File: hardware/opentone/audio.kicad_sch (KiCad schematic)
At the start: 29 parts

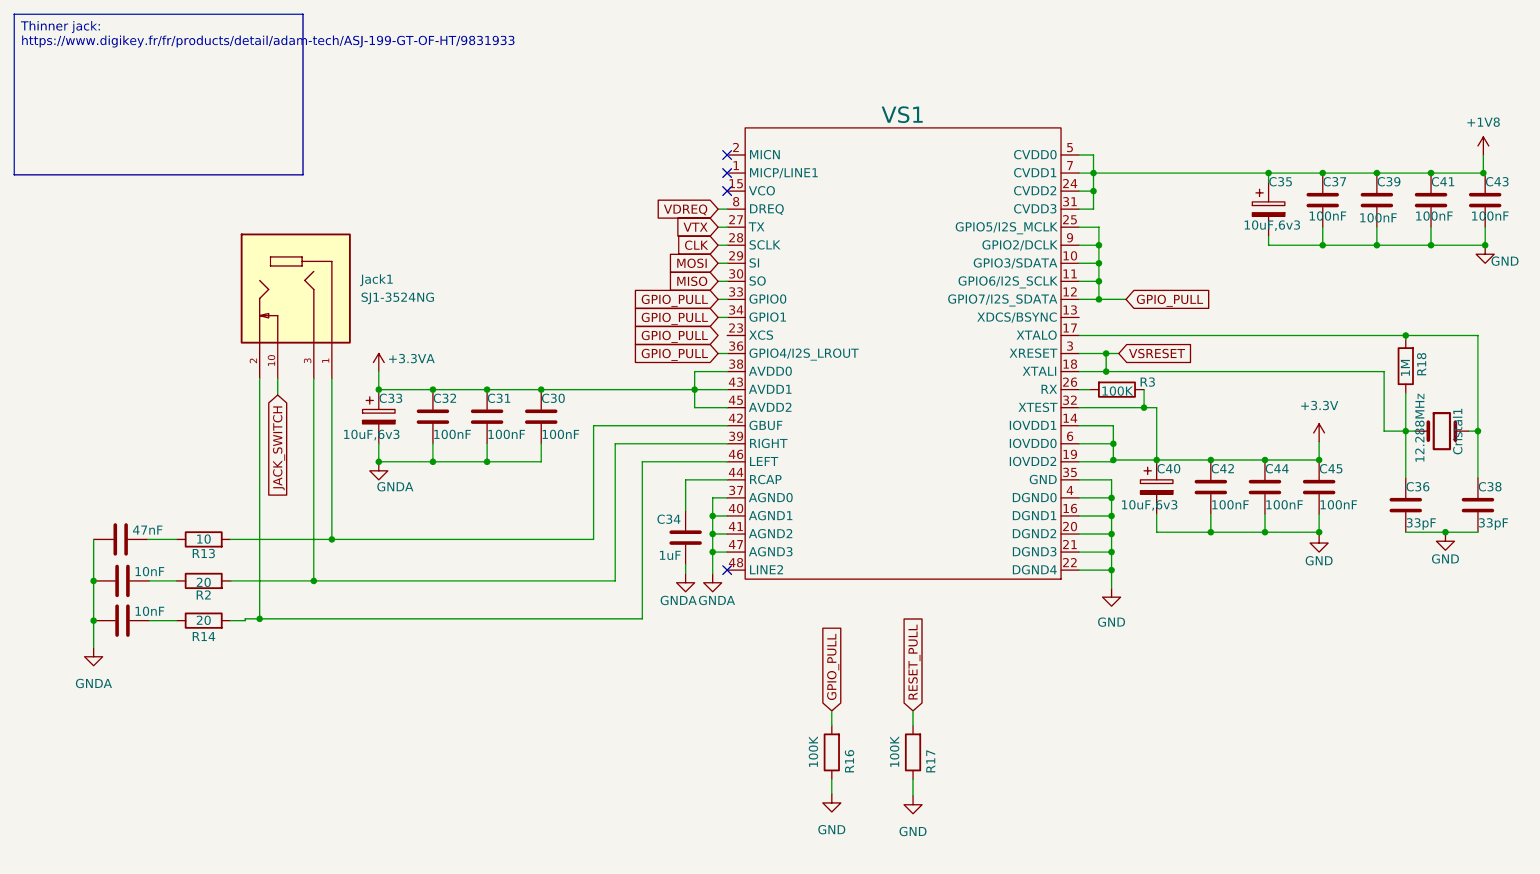
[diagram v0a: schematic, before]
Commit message: devboard audio and bluetooth schema
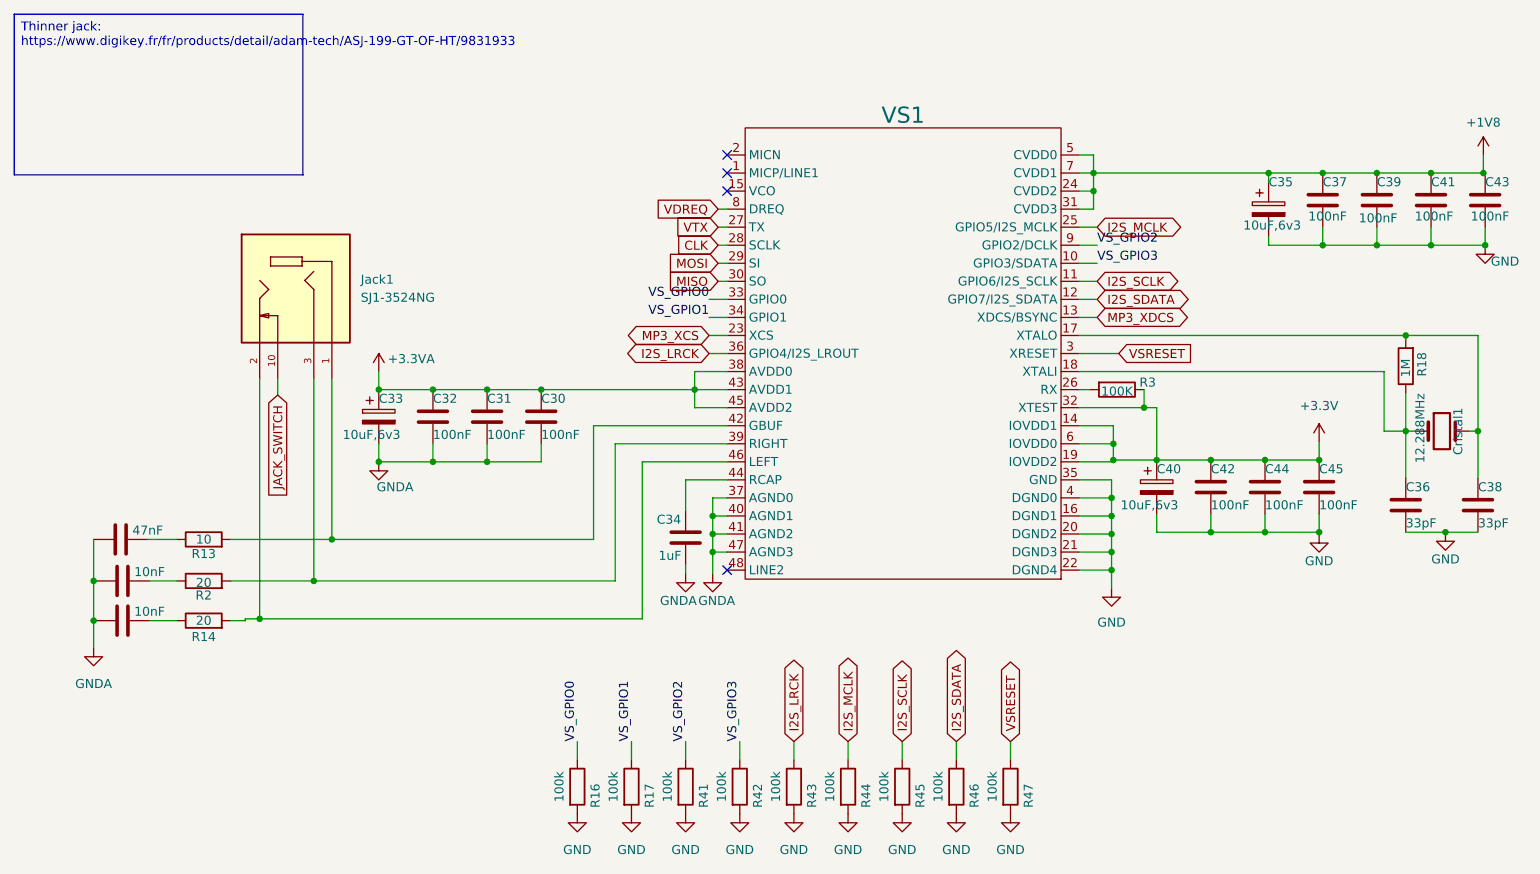
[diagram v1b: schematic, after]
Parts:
- added R41, R42, R43, R44, R45, R46, R47: 100k, symbol Device:R
- R16, R17: value 100K -> 100k
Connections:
- net RESET_PULL is gone; now on net GND: R17.2
- net GND: now also R16.2, R41.2, R42.2, R43.2, R44.2, R45.2, R46.2, R47.2; no longer R16.1, R17.1
- net VSRESET: now also R47.1; no longer C36.1, Cristal1.1, R18.1, VS1.18 (XTALI)
- net MP3_XDCS: now reaches VS1.13 (XDCS/BSYNC)
- net MP3_XCS: now reaches VS1.23 (XCS)
- removed net GPIO_PULL: R16.2, VS1.10 (GPIO3/SDATA), VS1.11 (GPIO6/I2S_SCLK), VS1.12 (GPIO7/I2S_SDATA), VS1.25 (GPIO5/I2S_MCLK), VS1.33 (GPIO0), VS1.34 (GPIO1), VS1.36 (GPIO4/I2S_LROUT), VS1.9 (GPIO2/DCLK)
- new net: C36.1, Cristal1.1, R18.1, VS1.18 (XTALI)
- new net I2S_LRCK: R43.1, VS1.36 (GPIO4/I2S_LROUT)
- new net I2S_MCLK: R44.1, VS1.25 (GPIO5/I2S_MCLK)
- new net I2S_SCLK: R45.1, VS1.11 (GPIO6/I2S_SCLK)
- new net I2S_SDATA: R46.1, VS1.12 (GPIO7/I2S_SDATA)
- new net VS_GPIO0: R16.1, VS1.33 (GPIO0)
- new net VS_GPIO1: R17.1, VS1.34 (GPIO1)
- new net VS_GPIO2: R41.1, VS1.9 (GPIO2/DCLK)
- new net VS_GPIO3: R42.1, VS1.10 (GPIO3/SDATA)

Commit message: wiring main MCU
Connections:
- net CLK renamed SPI2_SCK
- net JACK_SWITCH renamed HP1_DET
- net MISO renamed SPI2_MISO
- net MOSI renamed SPI2_MOSI
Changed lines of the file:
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@@
 		)
 	)
-	(global_label "CLK"
+	(global_label "SPI2_SCK"
 		(shape input)
 		(at 134.112 63.5 180)
@@
 		)
 	)
-	(global_label "MOSI"
+	(global_label "SPI2_MOSI"
 		(shape input)
 		(at 134.112 66.04 180)
@@
 		)
 	)
-	(global_label "JACK_SWITCH"
+	(global_label "HP1_DET"
 		(shape input)
 		(at 72.136 84.582 270)
@@
 		)
 	)
-	(global_label "MISO"
+	(global_label "SPI2_MISO"
 		(shape input)
 		(at 134.112 68.58 180)

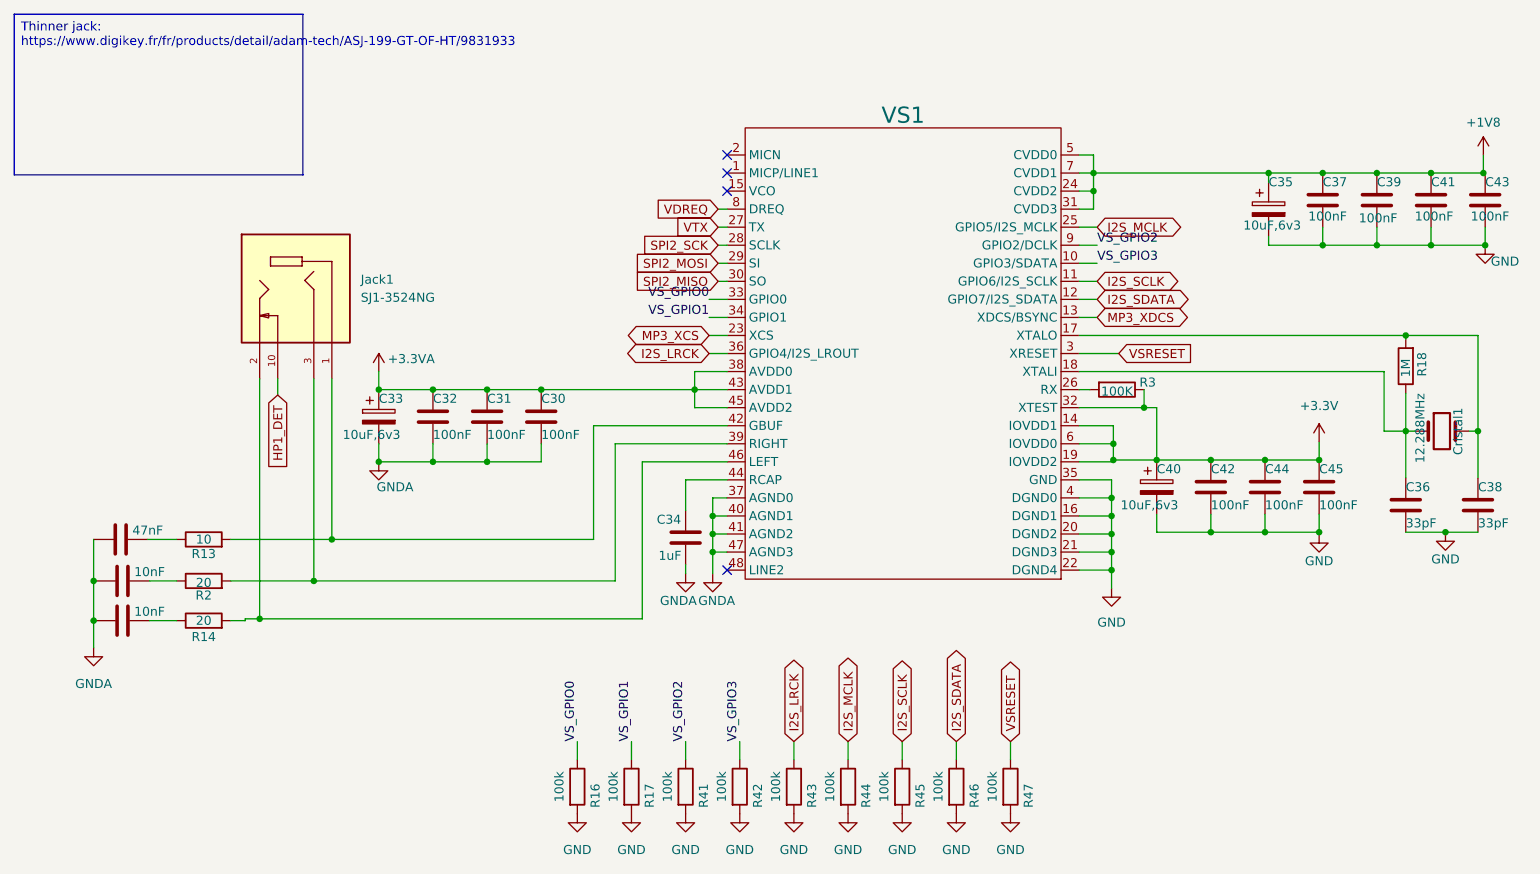
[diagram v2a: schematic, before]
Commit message: added sd card, haptic, updated old parts and set a datasheet and MPN to all parts
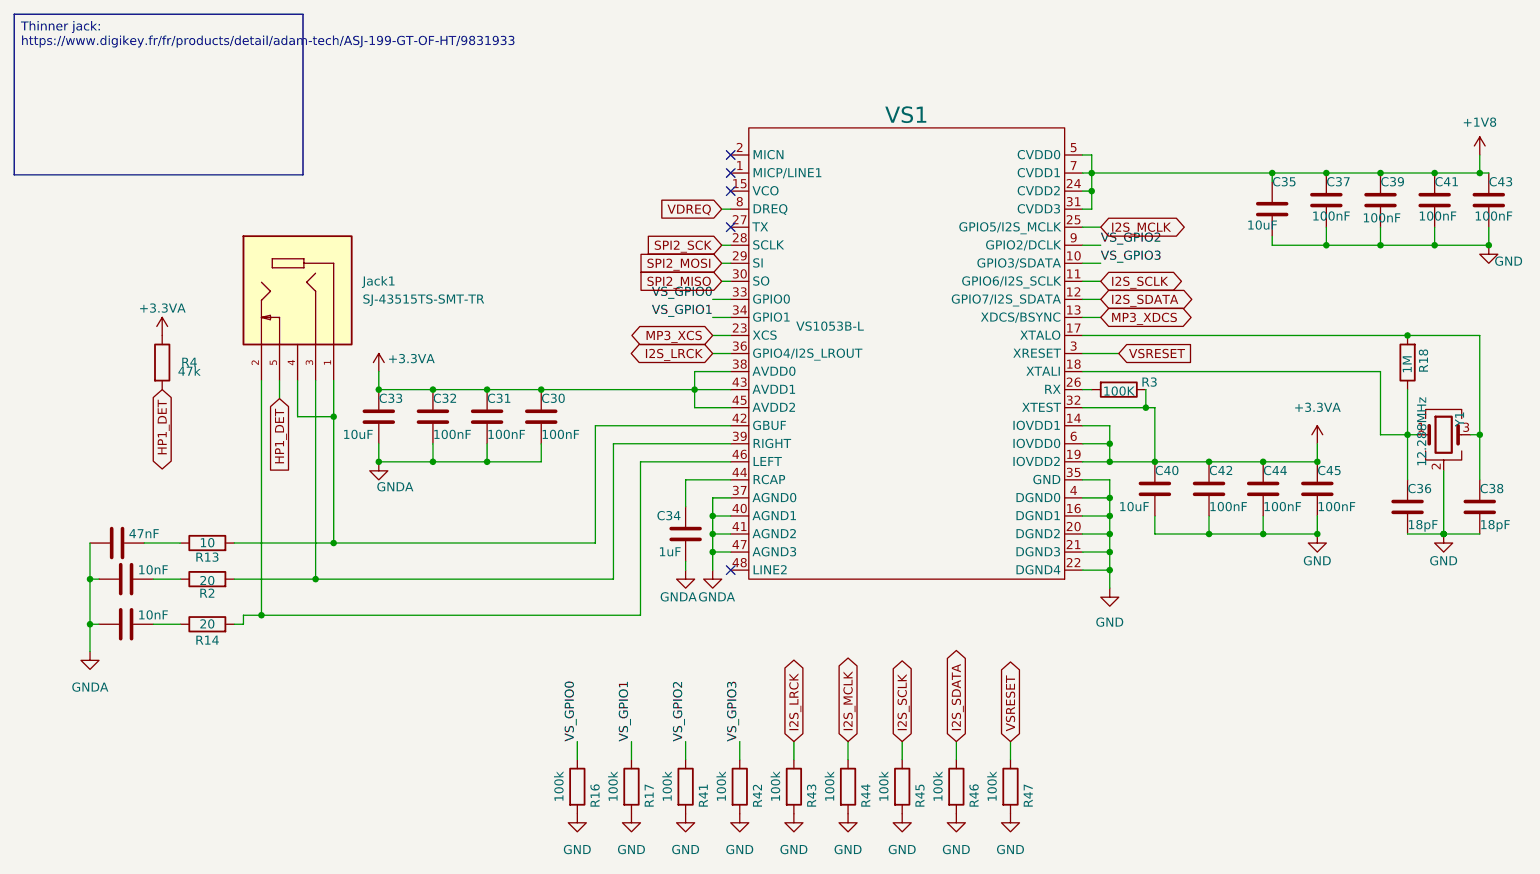
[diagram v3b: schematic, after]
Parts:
- added R4: 47k, Resistor_SMD:R_0603_1608Metric, symbol Device:R
- C29, C3: footprint (none) -> Capacitor_SMD:C_0603_1608Metric; LCSC (none) -> C85973; Manufacturer (none) -> Murata; Part number (none) -> GRM1885C1H103JA01D
- C30, C31, C32, C37, C39, C41, C42, C43, C44, C45: footprint (none) -> Capacitor_SMD:C_0603_1608Metric; LCSC (none) -> C14663; Manufacturer (none) -> YAGEO; Part number (none) -> CC0603KRX7R9BB104
- C33, C35, C40: value 10uF,6v3 -> 10uF; footprint (none) -> Capacitor_SMD:C_0603_1608Metric; symbol Device:C_Polarized -> Device:C; LCSC (none) -> C19702; Manufacturer (none) -> Samsung Electro-Mechanics; Part number (none) -> CL10A106KP8NNNC
- C34: footprint (none) -> Capacitor_SMD:C_0603_1608Metric; LCSC (none) -> C15849; Manufacturer (none) -> Samsung Electro-Mechanics; Part number (none) -> CL10A105KB8NNNC
- C36, C38: value 33pF -> 18pF; footprint (none) -> Capacitor_SMD:C_0603_1608Metric; LCSC (none) -> C1647; Manufacturer (none) -> Samsung Electro-Mechanics; Part number (none) -> CL10C180JB8NNNC
- C9: footprint (none) -> Capacitor_SMD:C_1206_3216Metric; LCSC (none) -> C21812; Manufacturer (none) -> Murata; Part number (none) -> GRM31M5C1H473JA01L
- Jack1: value SJ1-3524NG -> SJ-43515TS-SMT-TR; footprint opentone:CUI_SJ1-3524NG -> opentone:CUI_SJ-43515TS-SMT-TR; symbol opentone:SJ1-3524NG -> opentone:SJ-43515TS-SMT-TR; LCSC (none) -> C5353507; Part number SJ1-3524NG -> SJ-43515TS-SMT-TR
- R13: footprint (none) -> Resistor_SMD:R_0603_1608Metric; LCSC (none) -> C22859; Manufacturer (none) -> UNI-ROYAL; Part number (none) -> 0603WAF100JT5E
- R14, R2: footprint (none) -> Resistor_SMD:R_0603_1608Metric; LCSC (none) -> C22950; Manufacturer (none) -> UNI-ROYAL; Part number (none) -> 0603WAF200JT5E
- R16, R17, R3, R41, R42, R43, R44, R45, R46, R47: footprint (none) -> Resistor_SMD:R_0603_1608Metric; LCSC (none) -> C25803; Manufacturer (none) -> UNI-ROYAL; Part number (none) -> 0603WAF1003T5E
- R18: footprint (none) -> Resistor_SMD:R_0603_1608Metric; LCSC (none) -> C22935; Manufacturer (none) -> UNI-ROYAL; Part number (none) -> 0603WAF1004T5E
- VS1: value ~ -> VS1053B-L; footprint (none) -> Package_QFP:LQFP-48_7x7mm_P0.5mm; LCSC (none) -> C9922; Manufacturer (none) -> VLSI Solution; Part number (none) -> VS1053B-L
- Y1: renamed from Cristal1; footprint (none) -> Crystal:Crystal_SMD_3225-4Pin_3.2x2.5mm; symbol Device:Crystal -> Device:Crystal_GND24; LCSC (none) -> C362472; Manufacturer (none) -> Yajingxin; Part number (none) -> TXM12.288M0004322FBCDO00T
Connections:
- net +3.3V is gone; now on net +3.3VA: C40.1, C42.1, C44.1, C45.1, R3.1, VS1.14 (IOVDD1), VS1.19 (IOVDD2), VS1.32 (XTEST), VS1.6 (IOVDD0)
- net +3.3VA: now also R4.1
- net GND: now also Y1.2 (G), Y1.4 (G)
- net HP1_DET: now also Jack1.5, R4.2; no longer Jack1.10
- net at C38.1, R18.2, VS1.17 (XTALO): now also Y1.3; no longer Y1.2
- net at Jack1.1, R13.2, VS1.42 (GBUF): now also Jack1.4
- net VTX: no longer names the net of VS1.27 (TX)
- no-connect marks 4 -> 5
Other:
- moved on the sheet: C34, C37, C39, C41, C43, R13, R14, R18, R2, VS1

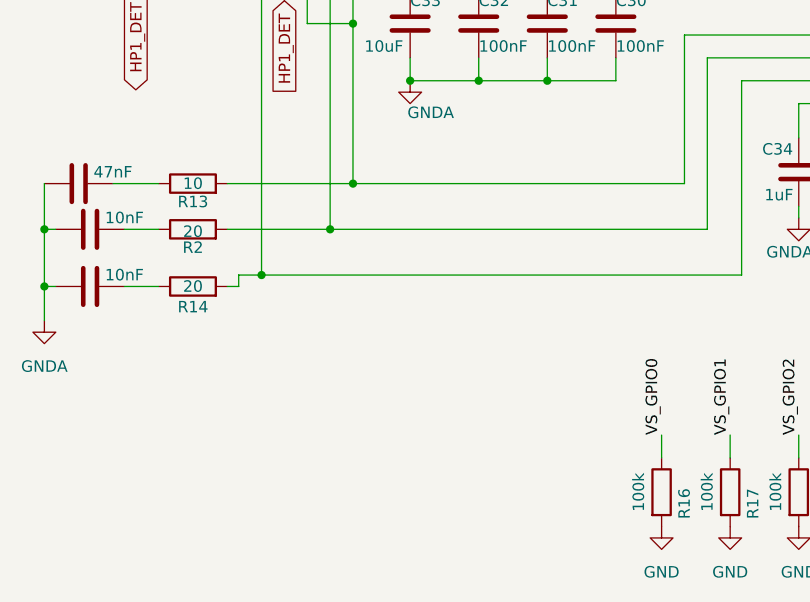
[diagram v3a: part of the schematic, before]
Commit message: added recommendations from Teel s checklists
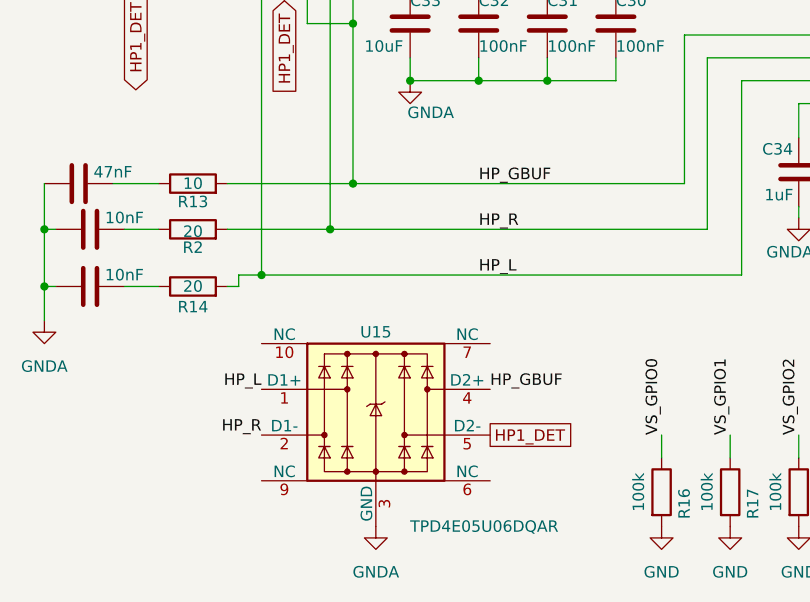
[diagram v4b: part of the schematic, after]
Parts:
- added U15: TPD4E05U06DQAR, Package_SON:USON-10_2.5x1.0mm_P0.5mm, symbol Power_Protection:TPD4E05U06DQA
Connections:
- net GNDA: now also U15.3 (GND), U15.8 (GND)
- net HP1_DET: now also U15.5 (D2-)
- net HP_R: now reaches Jack1.3, R2.2, VS1.39 (RIGHT)
- net HP_R: now also U15.2 (D1-)
- net HP_GBUF: now reaches Jack1.1, Jack1.4, R13.2, VS1.42 (GBUF)
- net HP_GBUF: now also U15.4 (D2+)
- net HP_L: now reaches Jack1.2, R14.2, VS1.46 (LEFT)
- net HP_L: now also U15.1 (D1+)

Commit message: updated BOM
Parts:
- R13: value 10 -> 10R
- R14, R2: value 20 -> 20R
- R3: value 100K -> 100k
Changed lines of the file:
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@@
 			)
 		)
-		(property "Value" "20"
+		(property "Value" "20R"
 			(at 62.23 110.744 90)
 			(show_name no)
@@
 			)
 		)
-		(property "Value" "10"
+		(property "Value" "10R"
 			(at 62.23 105.41 90)
 			(show_name no)
@@
 			)
 		)
-		(property "Value" "20"
+		(property "Value" "20R"
 			(at 62.23 116.84 90)
 			(show_name no)
@@
 			)
 		)
-		(property "Value" "100K"
+		(property "Value" "100k"
 			(at 190.5 84.074 90)
 			(show_name no)
